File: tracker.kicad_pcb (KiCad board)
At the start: 2 copper layers, 55.9 x 46.4 mm, 46 parts, among them J1 USB_C_Receptacle_USB2.0, J2 BAT, Q1 UMH3N, SW1 SW_Push, SW2 PWR_SW, U1 TP4056, U2 BNO055, U3 CH340C, U4 DW01, U5 FS8205A, U6 ESP-12F, U7 TPS63001, Y1 32.768 Khz

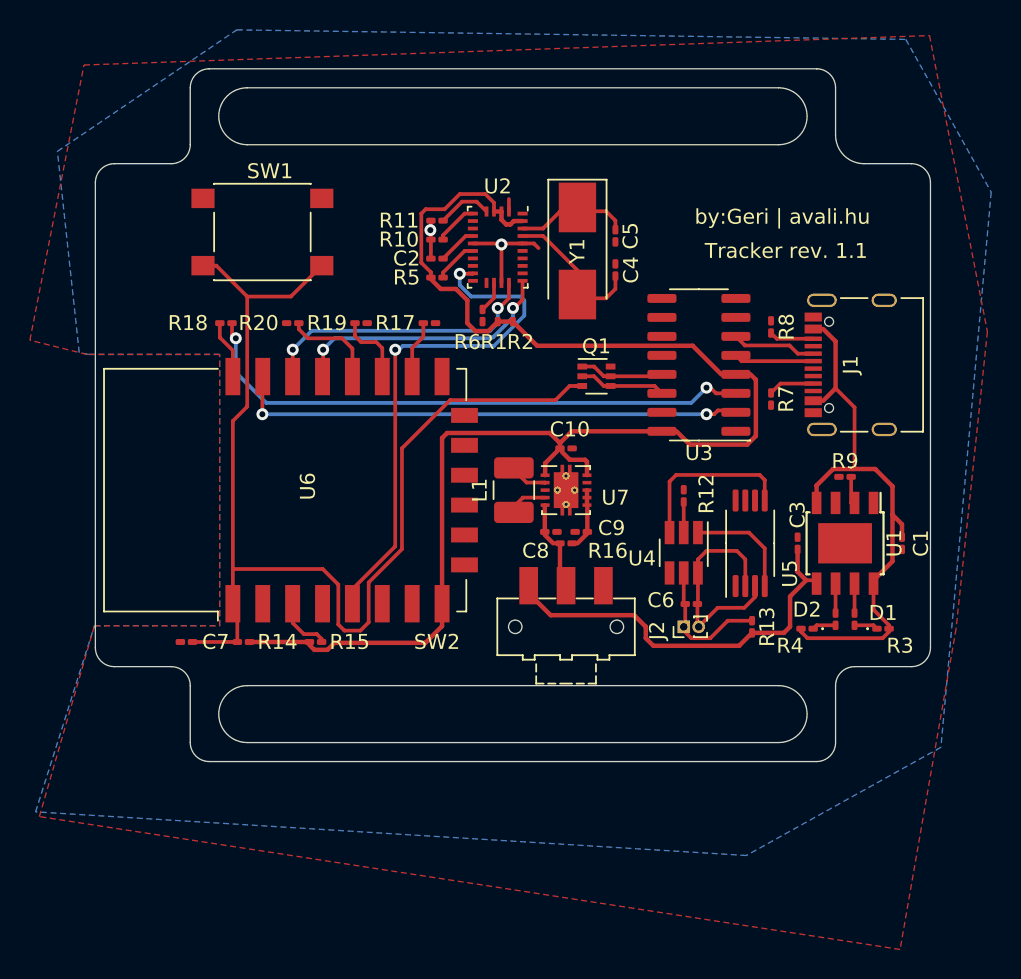
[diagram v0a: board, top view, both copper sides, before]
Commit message: metric/imperial fix
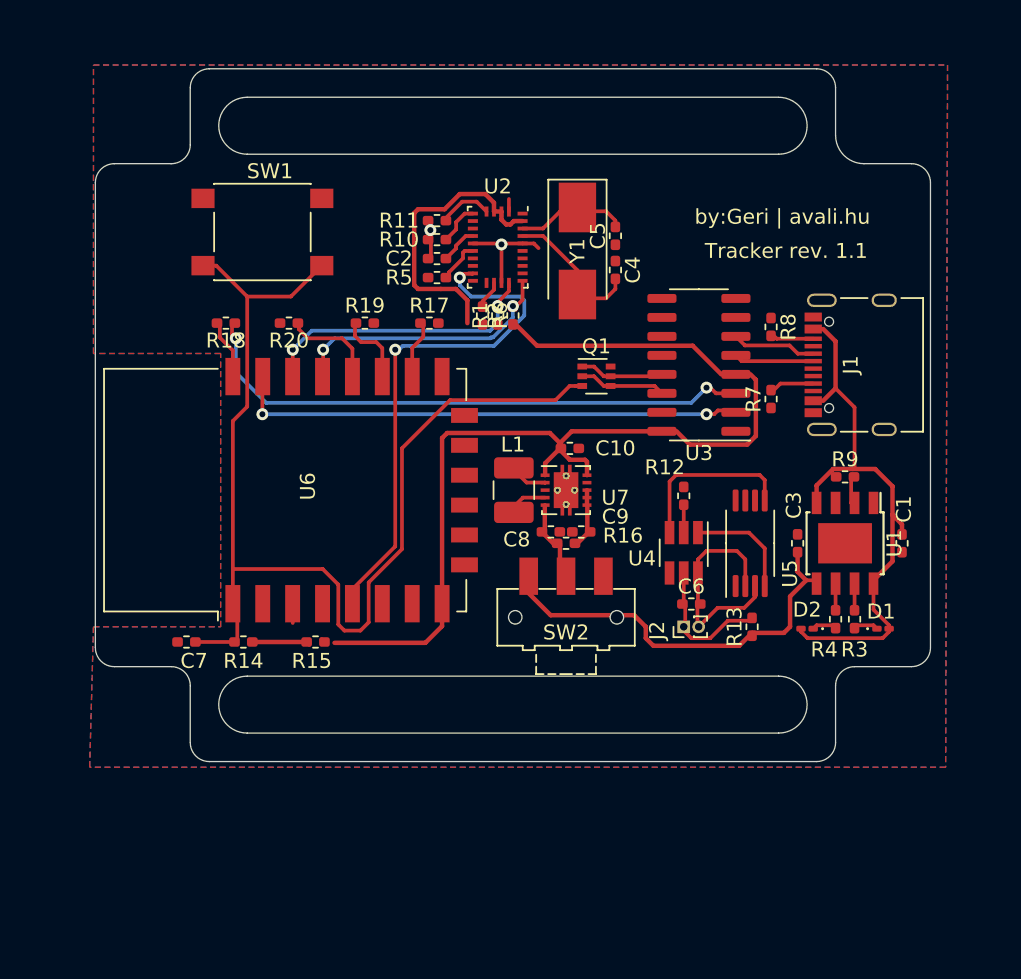
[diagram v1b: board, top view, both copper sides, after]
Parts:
- C1, C10, C2, C3, C4, C5, C6, C7, C8, C9: footprint Capacitor_SMD:C_0201_0603Metric_Pad0.64x0.40mm_HandSolder -> Resistor_SMD:R_0402_1005Metric_Pad0.72x0.64mm_HandSolder
- R1, R10, R11, R12, R13, R14, R15, R16, R17, R18, R19, R2, R20, R3, R4, R5, R6, R7, R8, R9: footprint Resistor_SMD:R_0201_0603Metric_Pad0.64x0.40mm_HandSolder -> Resistor_SMD:R_0402_1005Metric_Pad0.72x0.64mm_HandSolder
- moved SW2 0.63 mm to (164.8, 98.9)
- moved C10 0.25 mm to (165.1, 87.6)
- moved R19 0.25 mm to (151.4, 79.2)
- moved R20 0.25 mm to (146.3, 79.2)
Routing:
- net +3V3: track 97.8 -> 93.9 mm
- net Net-(R15-Pad2): track 3.87 -> 1.49 mm
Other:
- outline, holes or cut-outs redrawn

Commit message: a.
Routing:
- net GND: track 10.5 -> 25.2 mm, vias 2 -> 5
- net +3V3: track 93.9 -> 101.0 mm
- net Net-(R15-Pad2): track 1.49 -> 4.14 mm
- net Net-(C8-Pad2): track 6.26 -> 7.31 mm
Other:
- net class 03 added: clearance 0.2, trace_width 0.3, via_dia 0.8, via_drill 0.4
